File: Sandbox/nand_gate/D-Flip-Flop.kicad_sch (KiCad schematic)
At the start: 0 parts

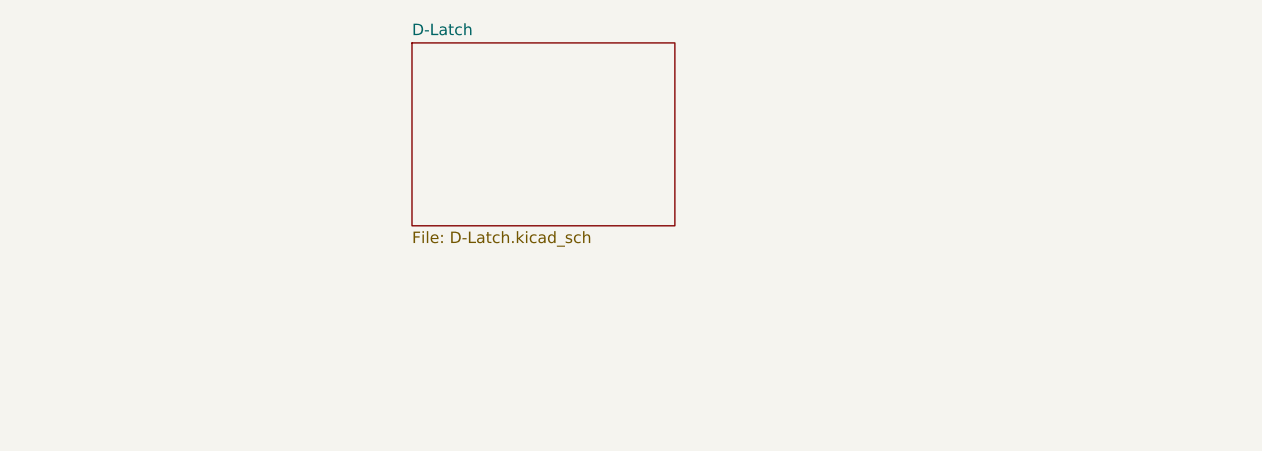
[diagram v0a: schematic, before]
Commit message: Added D Flip Flop
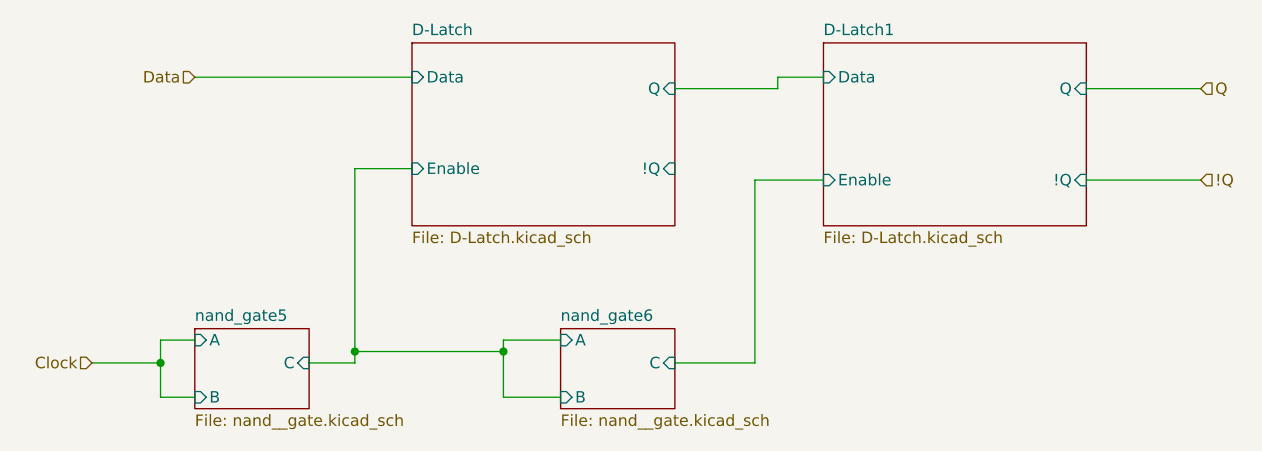
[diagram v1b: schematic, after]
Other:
- added sheet D-Latch1 (D-Latch.kicad_sch)
- added sheet nand_gate5 (nand__gate.kicad_sch)
- added sheet nand_gate6 (nand__gate.kicad_sch)
- sheet D-Latch ports: added !Q, Data, Enable, Q; removed none
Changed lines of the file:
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@@
 (kicad_sch (version 20230121) (generator eeschema)
   (paper "A4")
+  (junction (at 74.93 83.82) (diameter 0) (color 0 0 0 0)
+  )
+  (junction (at 36.83 85.09) (diameter 0) (color 0 0 0 0)
+  )
+  (junction (at 58.42 83.82) (diameter 0) (color 0 0 0 0)
+  )
+  (wire (pts (xy 40.64 82.55) (xy 36.83 82.55))
+    (stroke (width 0) (type default))
+  )
+  (wire (pts (xy 36.83 82.55) (xy 36.83 85.09))
+    (stroke (width 0) (type default))
+  )
+  (wire (pts (xy 58.42 85.09) (xy 58.42 83.82))
+    (stroke (width 0) (type default))
+  )
+  (wire (pts (xy 29.21 85.09) (xy 36.83 85.09))
+    (stroke (width 0) (type default))
+  )
+  (wire (pts (xy 93.98 85.09) (xy 102.87 85.09))
+    (stroke (width 0) (type default))
+  )
+  (wire (pts (xy 139.7 54.61) (xy 152.4 54.61))
+    (stroke (width 0) (type default))
+  )
+  (wire (pts (xy 81.28 88.9) (xy 74.93 88.9))
+    (stroke (width 0) (type default))
+  )
+  (wire (pts (xy 105.41 54.61) (xy 105.41 53.34))
+    (stroke (width 0) (type default))
+  )
+  (wire (pts (xy 93.98 54.61) (xy 105.41 54.61))
+    (stroke (width 0) (type default))
+  )
+  (wire (pts (xy 74.93 88.9) (xy 74.93 83.82))
+    (stroke (width 0) (type default))
+  )
+  (wire (pts (xy 36.83 85.09) (xy 36.83 88.9))
+    (stroke (width 0) (type default))
+  )
+  (wire (pts (xy 40.64 53.34) (xy 64.77 53.34))
+    (stroke (width 0) (type default))
+  )
+  (wire (pts (xy 74.93 82.55) (xy 81.28 82.55))
+    (stroke (width 0) (type default))
+  )
+  (wire (pts (xy 53.34 85.09) (xy 58.42 85.09))
+    (stroke (width 0) (type default))
+  )
+  (wire (pts (xy 58.42 83.82) (xy 58.42 63.5))
+    (stroke (width 0) (type default))
+  )
+  (wire (pts (xy 58.42 63.5) (xy 64.77 63.5))
+    (stroke (width 0) (type default))
+  )
+  (wire (pts (xy 58.42 83.82) (xy 74.93 83.82))
+    (stroke (width 0) (type default))
+  )
+  (wire (pts (xy 74.93 83.82) (xy 74.93 82.55))
+    (stroke (width 0) (type default))
+  )
+  (wire (pts (xy 139.7 64.77) (xy 152.4 64.77))
+    (stroke (width 0) (type default))
+  )
+  (wire (pts (xy 36.83 88.9) (xy 40.64 88.9))
+    (stroke (width 0) (type default))
+  )
+  (wire (pts (xy 105.41 53.34) (xy 110.49 53.34))
+    (stroke (width 0) (type default))
+  )
+  (wire (pts (xy 102.87 85.09) (xy 102.87 64.77))
+    (stroke (width 0) (type default))
+  )
+  (wire (pts (xy 102.87 64.77) (xy 110.49 64.77))
+    (stroke (width 0) (type default))
+  )
+  (hierarchical_label "Data" (shape input) (at 40.64 53.34 180) (fields_autoplaced)
+    (effects (font (size 1.27 1.27)) (justify right))
+  )
+  (hierarchical_label "Clock" (shape input) (at 29.21 85.09 180) (fields_autoplaced)
+    (effects (font (size 1.27 1.27)) (justify right))
+  )
+  (hierarchical_label "Q" (shape input) (at 152.4 54.61 0) (fields_autoplaced)
+    (effects (font (size 1.27 1.27)) (justify left))
+  )
+  (hierarchical_label "!Q" (shape input) (at 152.4 64.77 0) (fields_autoplaced)
+    (effects (font (size 1.27 1.27)) (justify left))
+  )
+  (sheet (at 81.28 81.28) (size 12.7 8.89) (fields_autoplaced)
+    (stroke (width 0.1524) (type solid))
+    (fill (color 0 0 0 0.0000))
+    (property "Sheetname" "nand_gate6" (at 81.28 80.5684 0)
+      (effects (font (size 1.27 1.27)) (justify left bottom))
+    )
+    (property "Sheetfile" "nand__gate.kicad_sch" (at 81.28 90.7546 0)
+      (effects (font (size 1.27 1.27)) (justify left top))
+    )
+    (pin "B" input (at 81.28 88.9 180)
+      (effects (font (size 1.27 1.27)) (justify left))
+    )
+    (pin "A" input (at 81.28 82.55 180)
+      (effects (font (size 1.27 1.27)) (justify left))
+    )
+    (pin "C" input (at 93.98 85.09 0)
+      (effects (font (size 1.27 1.27)) (justify right))
+    )
+    (instances
+      (project "nand_gate"
+        (path "/ae45e9d9-ebb5-4d6c-8dad-99eadd2be5c5/2e87dc14-878c-467c-8594-4a57b58f886f/6b230bbb-3b41-4fd2-a79b-e0cf50894ec7/0ad4044b-a9cd-452a-a5d6-d186c7bbd4c9" (page "5"))
+        (path "/ae45e9d9-ebb5-4d6c-8dad-99eadd2be5c5/2e87dc14-878c-467c-8594-4a57b58f886f/ec238f57-a4a9-49ac-b4d6-5b2cf534f59d/0ad4044b-a9cd-452a-a5d6-d186c7bbd4c9" (page "13"))
+        (path "/ae45e9d9-ebb5-4d6c-8dad-99eadd2be5c5/2e87dc14-878c-467c-8594-4a57b58f886f" (page "18"))
+      )
+    )
+  )
   (sheet (at 64.77 49.53) (size 29.21 20.32) (fields_autoplaced)
     (stroke (width 0.1524) (type solid))
@@
       (effects (font (size 1.27 1.27)) (justify left top))
     )
+    (pin "Data" input (at 64.77 53.34 180)
+      (effects (font (size 1.27 1.27)) (justify left))
+    )
+    (pin "Enable" input (at 64.77 63.5 180)
+      (effects (font (size 1.27 1.27)) (justify left))
+    )
+    (pin "!Q" input (at 93.98 63.5 0)
+      (effects (font (size 1.27 1.27)) (justify right))
+    )
+    (pin "Q" input (at 93.98 54.61 0)
+      (effects (font (size 1.27 1.27)) (justify right))
+    )
     (instances
       (project "nand_gate"
@@
       )
     )
+  )
+  (sheet (at 40.64 81.28) (size 12.7 8.89) (fields_autoplaced)
+    (stroke (width 0.1524) (type solid))
+    (fill (color 0 0 0 0.0000))
+    (property "Sheetname" "nand_gate5" (at 40.64 80.5684 0)
+      (effects (font (size 1.27 1.27)) (justify left bottom))
+    )
+    (property "Sheetfile" "nand__gate.kicad_sch" (at 40.64 90.7546 0)
+      (effects (font (size 1.27 1.27)) (justify left top))
+    )
+    (pin "B" input (at 40.64 88.9 180)
+      (effects (font (size 1.27 1.27)) (justify left))
+    )
+    (pin "A" input (at 40.64 82.55 180)
+      (effects (font (size 1.27 1.27)) (justify left))
+    )
+    (pin "C" input (at 53.34 85.09 0)
+      (effects (font (size 1.27 1.27)) (justify right))
+    )
+    (instances
+      (project "nand_gate"
+        (path "/ae45e9d9-ebb5-4d6c-8dad-99eadd2be5c5/2e87dc14-878c-467c-8594-4a57b58f886f/6b230bbb-3b41-4fd2-a79b-e0cf50894ec7/0ad4044b-a9cd-452a-a5d6-d186c7bbd4c9" (page "5"))
+        (path "/ae45e9d9-ebb5-4d6c-8dad-99eadd2be5c5/2e87dc14-878c-467c-8594-4a57b58f886f/ec238f57-a4a9-49ac-b4d6-5b2cf534f59d/0ad4044b-a9cd-452a-a5d6-d186c7bbd4c9" (page "13"))
+        (path "/ae45e9d9-ebb5-4d6c-8dad-99eadd2be5c5/2e87dc14-878c-467c-8594-4a57b58f886f" (page "17"))
+      )
+    )
+  )
+  (sheet (at 110.49 49.53) (size 29.21 20.32) (fields_autoplaced)
+    (stroke (width 0.1524) (type solid))
+    (fill (color 0 0 0 0.0000))
+    (property "Sheetname" "D-Latch1" (at 110.49 48.8184 0)
+      (effects (font (size 1.27 1.27)) (justify left bottom))
+    )
+    (property "Sheetfile" "D-Latch.kicad_sch" (at 110.49 70.4346 0)
+      (effects (font (size 1.27 1.27)) (justify left top))
+    )
+    (pin "Data" input (at 110.49 53.34 180)
+      (effects (font (size 1.27 1.27)) (justify left))
+    )
+    (pin "Enable" input (at 110.49 64.77 180)
+      (effects (font (size 1.27 1.27)) (justify left))
+    )
+    (pin "!Q" input (at 139.7 64.77 0)
+      (effects (font (size 1.27 1.27)) (justify right))
+    )
+    (pin "Q" input (at 139.7 54.61 0)
+      (effects (font (size 1.27 1.27)) (justify right))
+    )
+    (instances
+      (project "nand_gate"
+        (path "/ae45e9d9-ebb5-4d6c-8dad-99eadd2be5c5/2e87dc14-878c-467c-8594-4a57b58f886f" (page "10"))
+      )
+    )
